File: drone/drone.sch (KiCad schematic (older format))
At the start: 20 parts, among them IC1 AT89S4051-P, K1 RELAY_2RT, K2 RELAY_2RT, P1 ISP, P2 LeftM, P3 RightM, P4 Blade1, P5 Blade2, Q1 NPN, Q2 NPN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

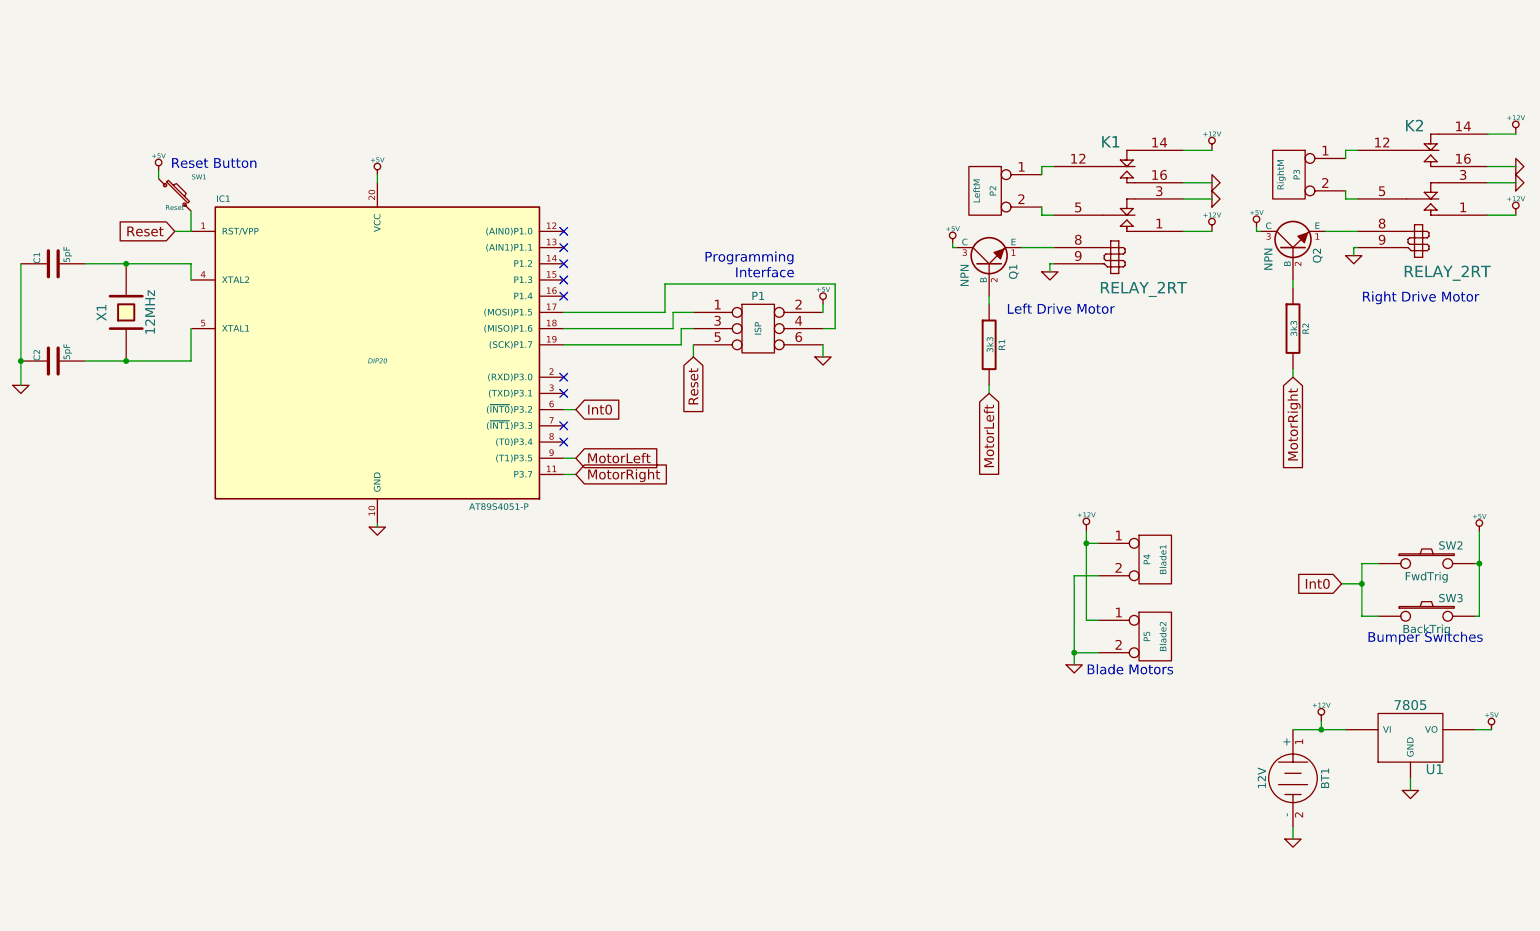
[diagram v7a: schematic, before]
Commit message: Worked on the drone schematic
* It is really difficult to get relays that are cheap as such
    the motor control was switched using an H-Bridge Configuration
    to control motor state and direction
* Added a bunch of symbols to the cache library.
    * Relays and lots of them.
* Started work on the netlist
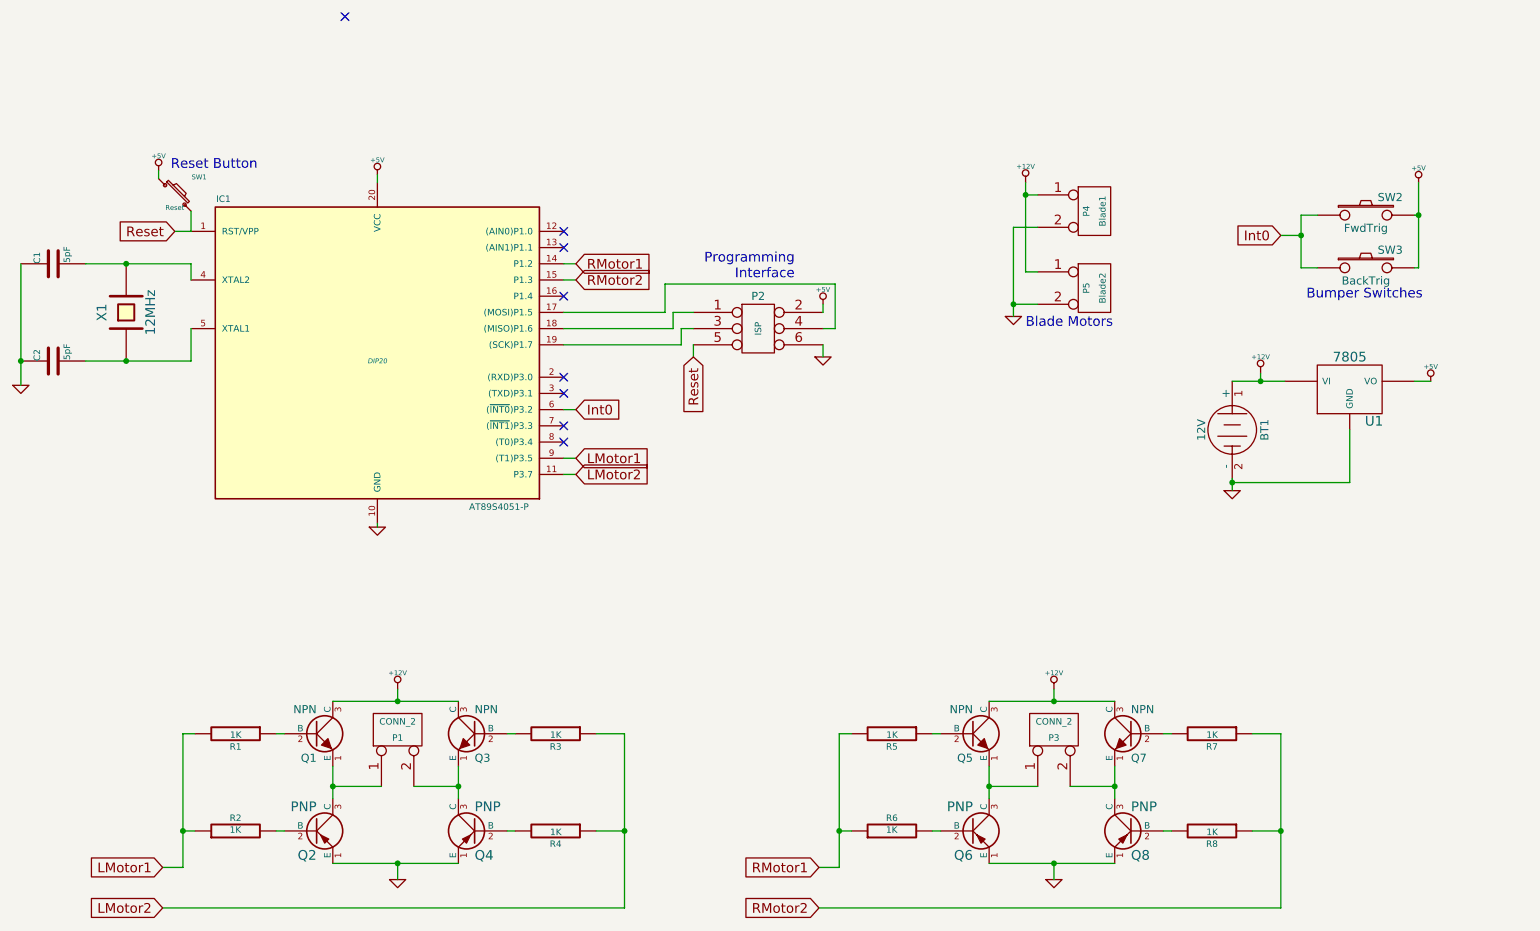
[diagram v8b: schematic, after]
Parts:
- removed K1, K2: RELAY_2RT, symbol RELAY_2RT
- removed P2: LeftM, symbol CONN_2
- removed Q2: NPN, symbol NPN
- added P1: CONN_2, symbol CONN_2
- added Q2, Q4, Q6, Q8: PNP, symbol PNP
- added Q3, Q5, Q7: NPN, symbol NPN
- added R3, R4, R5, R6, R7, R8: 1K, symbol R
- P3: value RightM -> CONN_2
- R1, R2: value 3k3 -> 1K
- renumbered P1 to P2
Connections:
- net MotorLeft is gone; now on net LMotor1: IC1.9 ((T1)P3.5), R1.2
- net +12V: now also Q1.3 (C), Q3.3 (C), Q5.3 (C), Q7.3 (C)
- net +5V: no longer Q1.3 (C)
- net GND: now also Q2.1 (E), Q4.1 (E), Q6.1 (E), Q8.1 (E)
- net RMotor1: now reaches IC1.14 (P1.2)
- net RMotor1: now also R5.2, R6.1
- net RMotor2: now reaches IC1.15 (P1.3)
- net RMotor2: now also R7.1, R8.1
- net at P3.1 (P1): now also Q5.1 (E), Q6.3 (C)
- net at P3.2 (PM): now also Q7.1 (E), Q8.3 (C)
- net LMotor1: now reaches R2.1
- net at Q1.1 (E): now also P1.1 (P1), Q2.3 (C)
- net MotorRight: no longer names the net of R2.2
- net MotorRight: now also Q2.2 (B); no longer IC1.11 (P3.7)
- new net: P1.2 (PM), Q3.1 (E), Q4.3 (C)
- new net: Q3.2 (B), R3.2
- new net: Q4.2 (B), R4.2
- new net: Q5.2 (B), R5.1
- new net: Q7.2 (B), R7.2
- new net: Q6.2 (B), R6.2
- new net: Q8.2 (B), R8.2
- new net LMotor2: IC1.11 (P3.7), R3.1, R4.1
- no-connect marks 9 -> 8
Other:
- note removed: "Left Drive Motor"
- note removed: "Right Drive Motor"
- moved on the sheet: BT1, P4, P5, SW2, SW3, U1
